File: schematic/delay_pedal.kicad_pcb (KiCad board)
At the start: 4 copper layers, 110 x 50 mm, 149 parts, among them J1 IN Gain, J10 VFLASH, J12 LP, J13 Mix, J14 OUT Gain, J3 SPI FLASH, J4 Audio In, J5 FDBK, J6 +9V, J8 Time, J9 Audio Out, SW1 RESET, SW2 SW_SPST, U1 ICE40LP1K-QN84, U10 TPL810ADJ-5TR, U11 TPL810F50-89TR, U12 ADS8339IDGSR, U13 TLV76033DBZR, U14 OPA1678, U15 DAC8551IADGKR, U16 REF5045AD, U17 OPA1678, U2 APS1604M-3SQR, U3 OPA1678, U4 NXB0104, U5 OPA1678, U6 W25X20CLSN, U8 OPA1678, U9 OPA1678, X1 KXO-V96T

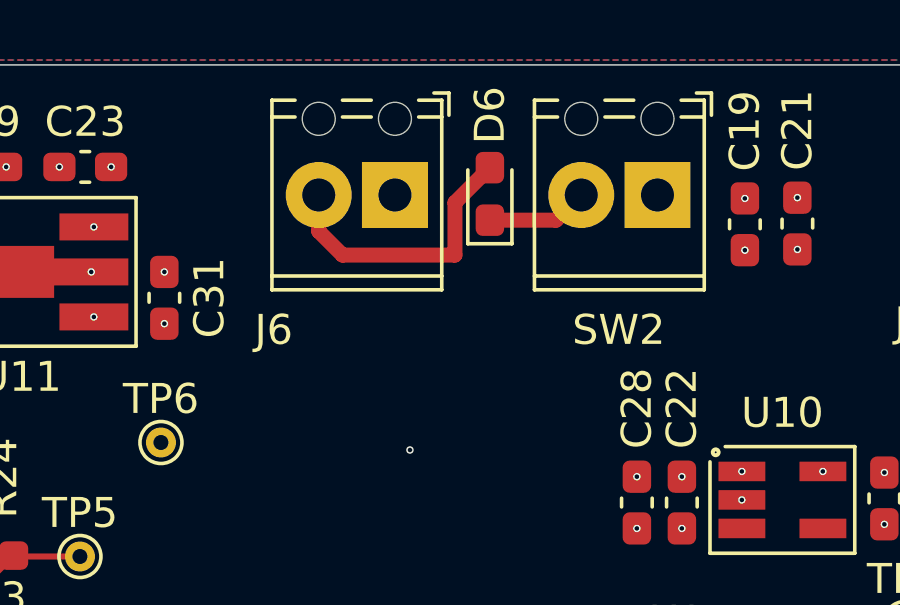
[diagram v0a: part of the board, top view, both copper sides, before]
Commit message: Updated Schottky diode footprint
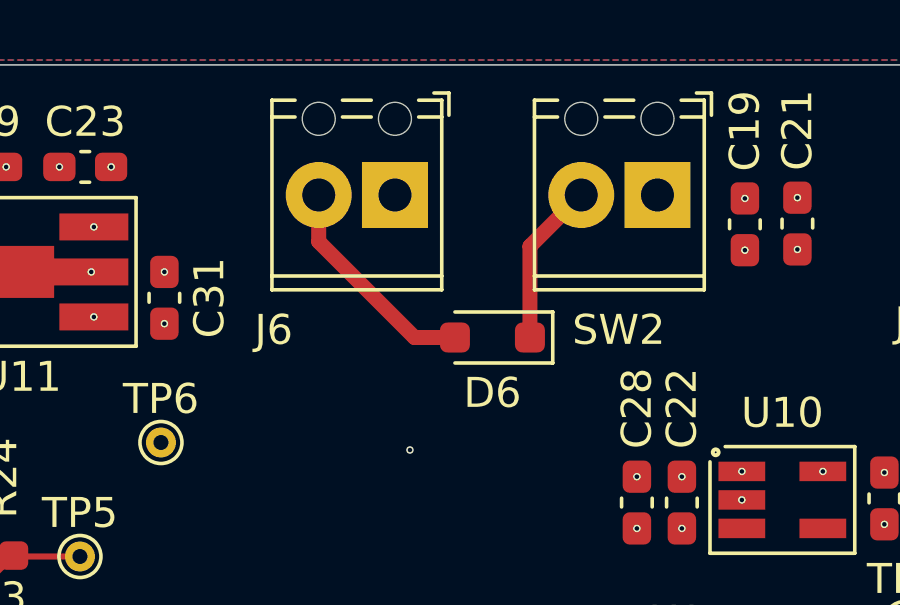
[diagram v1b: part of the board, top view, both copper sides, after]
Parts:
- D6: footprint Diode_SMD:D_0603_1608Metric_Pad1.05x0.95mm_HandSolder -> Diode_SMD:D_SOD-323_HandSoldering
- moved D6 4.79 mm to (166.2, 84.0), turned to 180 degrees
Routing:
- net Net-(D6-K): track 3.31 -> 5.49 mm
- net /+9V: track 10.1 -> 8.09 mm
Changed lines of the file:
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@@
 		)
 	)
-	(footprint "Diode_SMD:D_0603_1608Metric_Pad1.05x0.95mm_HandSolder"
+	(footprint "Diode_SMD:D_SOD-323_HandSoldering"
 		(layer "F.Cu")
-		(at 166.164214 79.214214 90)
-		(descr "Diode SMD 0603 (1608 Metric), square (rectangular) end terminal, IPC_7351 nominal, (Body size source: http://www.tortai-tech.com/upload/download/2011102023233369053.pdf), generated with kicad-footprint-generator")
-		(tags "diode handsolder")
+		(at 166.25 84 180)
+		(descr "SOD-323")
+		(tags "SOD-323")
 		(property "Reference" "D6"
-			(at 2.625 0 90)
+			(at 0 -1.85 360)
 			(layer "F.SilkS")
 			(effects
@@
 		)
 		(property "Value" "Schottky"
-			(at 0 1.43 90)
+			(at 0.1 1.9 360)
 			(layer "F.Fab")
 			(hide yes)
@@
 			)
 		)
-		(property "Footprint" "Diode_SMD:D_0603_1608Metric_Pad1.05x0.95mm_HandSolder"
-			(at 0 0 90)
+		(property "Footprint" "Diode_SMD:D_SOD-323_HandSoldering"
+			(at 0 0 180)
 			(unlocked yes)
 			(layer "F.Fab")
@@
 		)
 		(property "Datasheet" ""
-			(at 0 0 90)
+			(at 0 0 180)
 			(unlocked yes)
 			(layer "F.Fab")
@@
 		)
 		(property "Description" "Schottky diode, Generic Symbol, Alternate KiCAD Library"
-			(at 0 0 90)
+			(at 0 0 180)
 			(unlocked yes)
 			(layer "F.Fab")
@@
 		(attr smd)
 		(fp_line
-			(start 0.8 -0.735)
-			(end -1.66 -0.735)
+			(start -2.01 0.85)
+			(end 1.25 0.85)
 			(stroke
 				(width 0.12)
@@
 		)
 		(fp_line
-			(start -1.66 -0.735)
-			(end -1.66 0.735)
+			(start -2.01 -0.85)
+			(end 1.25 -0.85)
 			(stroke
 				(width 0.12)
@@
 		)
 		(fp_line
-			(start -1.66 0.735)
-			(end 0.8 0.735)
+			(start -2.01 -0.85)
+			(end -2.01 0.85)
 			(stroke
 				(width 0.12)
@@
 		)
 		(fp_line
-			(start 1.65 -0.73)
-			(end 1.65 0.73)
+			(start 2 -0.95)
+			(end 2 0.95)
 			(stroke
 				(width 0.05)
@@
 		)
 		(fp_line
-			(start -1.65 -0.73)
-			(end 1.65 -0.73)
+			(start -2 0.95)
+			(end 2 0.95)
 			(stroke
 				(width 0.05)
@@
 		)
 		(fp_line
-			(start 1.65 0.73)
-			(end -1.65 0.73)
+			(start -2 -0.95)
+			(end 2 -0.95)
 			(stroke
 				(width 0.05)
@@
 		)
 		(fp_line
-			(start -1.65 0.73)
-			(end -1.65 -0.73)
+			(start -2 -0.95)
+			(end -2 0.95)
 			(stroke
 				(width 0.05)
@@
 		)
 		(fp_line
-			(start 0.8 -0.4)
-			(end -0.5 -0.4)
+			(start 0.9 0.7)
+			(end -0.9 0.7)
 			(stroke
 				(width 0.1)
@@
 		)
 		(fp_line
-			(start -0.5 -0.4)
-			(end -0.8 -0.1)
+			(start 0.9 -0.7)
+			(end 0.9 0.7)
 			(stroke
 				(width 0.1)
@@
 		)
 		(fp_line
-			(start -0.8 -0.1)
-			(end -0.8 0.4)
+			(start 0.2 0.35)
+			(end -0.3 0)
 			(stroke
 				(width 0.1)
@@
 		)
 		(fp_line
-			(start 0.8 0.4)
-			(end 0.8 -0.4)
+			(start 0.2 0)
+			(end 0.45 0)
 			(stroke
 				(width 0.1)
@@
 		)
 		(fp_line
-			(start -0.8 0.4)
-			(end 0.8 0.4)
+			(start 0.2 -0.35)
+			(end 0.2 0.35)
+			(stroke
+				(width 0.1)
+				(type solid)
+			)
+			(layer "F.Fab")
+		)
+		(fp_line
+			(start -0.3 0)
+			(end 0.2 -0.35)
+			(stroke
+				(width 0.1)
+				(type solid)
+			)
+			(layer "F.Fab")
+		)
+		(fp_line
+			(start -0.3 0)
+			(end -0.5 0)
+			(stroke
+				(width 0.1)
+				(type solid)
+			)
+			(layer "F.Fab")
+		)
+		(fp_line
+			(start -0.3 -0.35)
+			(end -0.3 0.35)
+			(stroke
+				(width 0.1)
+				(type solid)
+			)
+			(layer "F.Fab")
+		)
+		(fp_line
+			(start -0.9 0.7)
+			(end -0.9 -0.7)
+			(stroke
+				(width 0.1)
+				(type solid)
+			)
+			(layer "F.Fab")
+		)
+		(fp_line
+			(start -0.9 -0.7)
+			(end 0.9 -0.7)
 			(stroke
 				(width 0.1)
@@
 		)
 		(fp_text user "${REFERENCE}"
-			(at 0 0 90)
+			(at 0 -1.85 360)
 			(layer "F.Fab")
 			(effects
 				(font
-					(size 0.4 0.4)
-					(thickness 0.06)
+					(size 1 1)
+					(thickness 0.15)
 				)
 			)
 		)
 		(pad "1" smd roundrect
-			(at -0.875 0 90)
-			(size 1.05 0.95)
+			(at -1.25 0 180)
+			(size 1 1)
 			(layers "F.Cu" "F.Paste" "F.Mask")
 			(roundrect_rratio 0.25)
@@
 		)
 		(pad "2" smd roundrect
-			(at 0.875 0 90)
-			(size 1.05 0.95)
+			(at 1.25 0 180)
+			(size 1 1)
 			(layers "F.Cu" "F.Paste" "F.Mask")
 			(roundrect_rratio 0.25)
@@
 			(pintype "passive")
 		)
-		(model "${KICAD8_3DMODEL_DIR}/Diode_SMD.3dshapes/D_0603_1608Metric.wrl"
+		(model "${KICAD8_3DMODEL_DIR}/Diode_SMD.3dshapes/D_SOD-323.wrl"
 			(offset
 				(xyz 0 0 0)
@@
 	)
 	(segment
-		(start 165 79.503428)
-		(end 165 81.2525)
-		(width 0.5)
-		(layer "F.Cu")
-		(net 32)
-	)
-	(segment
-		(start 160.46 80.46)
-		(end 160.46 79.25)
+		(start 163.654366 84)
+		(end 165 84)
 		(width 0.5)
 		(layer "F.Cu")
@@
 	)
 	(segment
-		(start 165 81.2525)
-		(end 161.2525 81.2525)
-		(width 0.5)
-		(layer "F.Cu")
-		(net 32)
-	)
-	(segment
-		(start 161.2525 81.2525)
-		(end 160.46 80.46)
+		(start 160.624214 79.299214)
+		(end 160.624214 78.625786)
 		(width 0.5)
 		(layer "F.Cu")
@@
 	)
 	(segment
-		(start 160.624214 79.299214)
-		(end 160.624214 78.625786)
+		(start 160.46 79.25)
+		(end 160.46 80.805634)
 		(width 0.5)
 		(layer "F.Cu")
@@
 	)
 	(segment
-		(start 166.164214 78.339214)
-		(end 165 79.503428)
+		(start 160.46 80.805634)
+		(end 163.654366 84)
 		(width 0.5)
 		(layer "F.Cu")
@@
 	)
 	(segment
-		(start 168.370786 80.089214)
-		(end 169.124214 79.335786)
+		(start 167.5 80.96)
+		(end 169.21 79.25)
 		(width 0.5)
 		(layer "F.Cu")
@@
 	)
 	(segment
-		(start 166.164214 80.089214)
-		(end 168.370786 80.089214)
+		(start 167.5 84)
+		(end 167.5 80.96)
 		(width 0.5)
 		(layer "F.Cu")

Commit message: Generated fabrication files
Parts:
- C19: footprint Capacitor_SMD:C_0603_1608Metric_Pad1.08x0.95mm_HandSolder -> Capacitor_THT:CP_Radial_D6.3mm_P2.50mm
- C40, C5, C60: footprint Capacitor_SMD:C_0603_1608Metric_Pad1.08x0.95mm_HandSolder -> Capacitor_SMD:C_1206_3216Metric_Pad1.33x1.80mm_HandSolder
- J1, J12, J14, J4, J5, J6, J9, SW2: footprint TerminalBlock_Phoenix:TerminalBlock_Phoenix_MPT-0,5-2-2.54_1x02_P2.54mm_Horizontal -> Connector_PinHeader_2.54mm:PinHeader_1x02_P2.54mm_Vertical
- J13: footprint TerminalBlock_Phoenix:TerminalBlock_Phoenix_MPT-0,5-3-2.54_1x03_P2.54mm_Horizontal -> Connector_PinHeader_2.54mm:PinHeader_1x03_P2.54mm_Vertical
- J8: footprint TerminalBlock_Phoenix:TerminalBlock_Phoenix_MPT-0,5-5-2.54_1x05_P2.54mm_Horizontal -> Connector_PinHeader_2.54mm:PinHeader_1x05_P2.54mm_Vertical
- U14, U17, U3, U5, U8, U9: value OPA1678 -> RC4580
- moved TP1 5.48 mm to (102.5, 112.7)
- moved C21 4.18 mm to (172.6, 82.0), turned to 0 degrees
- moved C19 3.40 mm to (178.0, 79.6), turned to -90 degrees
- moved J8 2.75 mm to (194.5, 79.2), turned to -90 degrees
- moved C60 1.78 mm to (151.9, 103.2), turned to 90 degrees
- moved C40 0.95 mm to (114.6, 90.2)
- moved C5 0.90 mm to (107.1, 109.8)
- turned J1 to 90 degrees
- turned J12 to 90 degrees
- turned J13 to 0 degrees
- turned J14 to -90 degrees
- turned J4 to 0 degrees
- turned J5 to 90 degrees
- turned J6 to -90 degrees
- turned J9 to 0 degrees
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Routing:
- net Net-(J12-Pin_1): track 27.5 -> 24.8 mm
- net Net-(J5-Pin_2): track 7.38 -> 5.90 mm
- net Net-(J14-Pin_2): track 13.3 -> 14.8 mm
- net Aref: track 22.2 -> 20.7 mm
- net /IN: track 13.8 -> 12.5 mm
- net /FLASH.SCK: track 22.8 -> 21.7 mm
- net /FLASH.SDI: track 22.0 -> 21.1 mm
- net Net-(U3A-+): track 5.63 -> 6.41 mm
- net /FLASH.SDO: track 24.1 -> 24.8 mm
- net /OUT: track 22.7 -> 22.2 mm
- net Vs: vias 26 -> 25

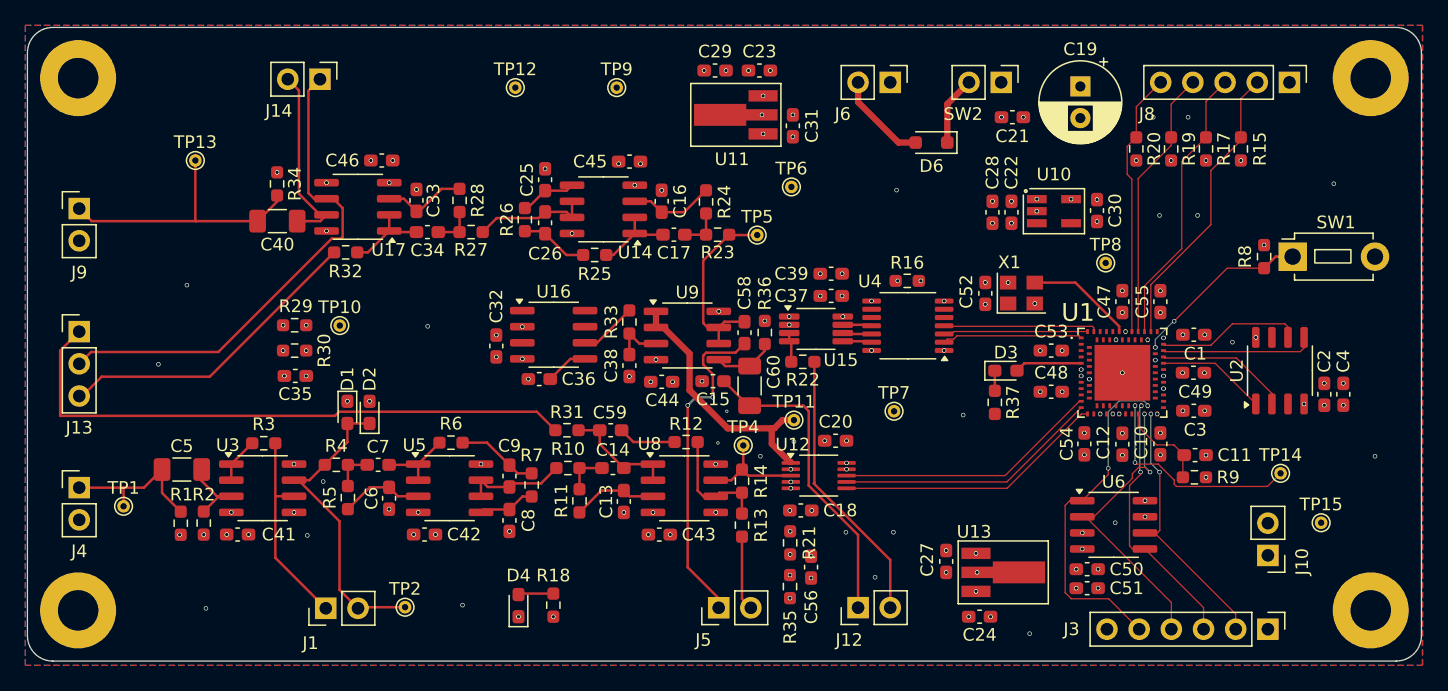
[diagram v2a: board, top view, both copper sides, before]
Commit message: Fixed footprint assignments
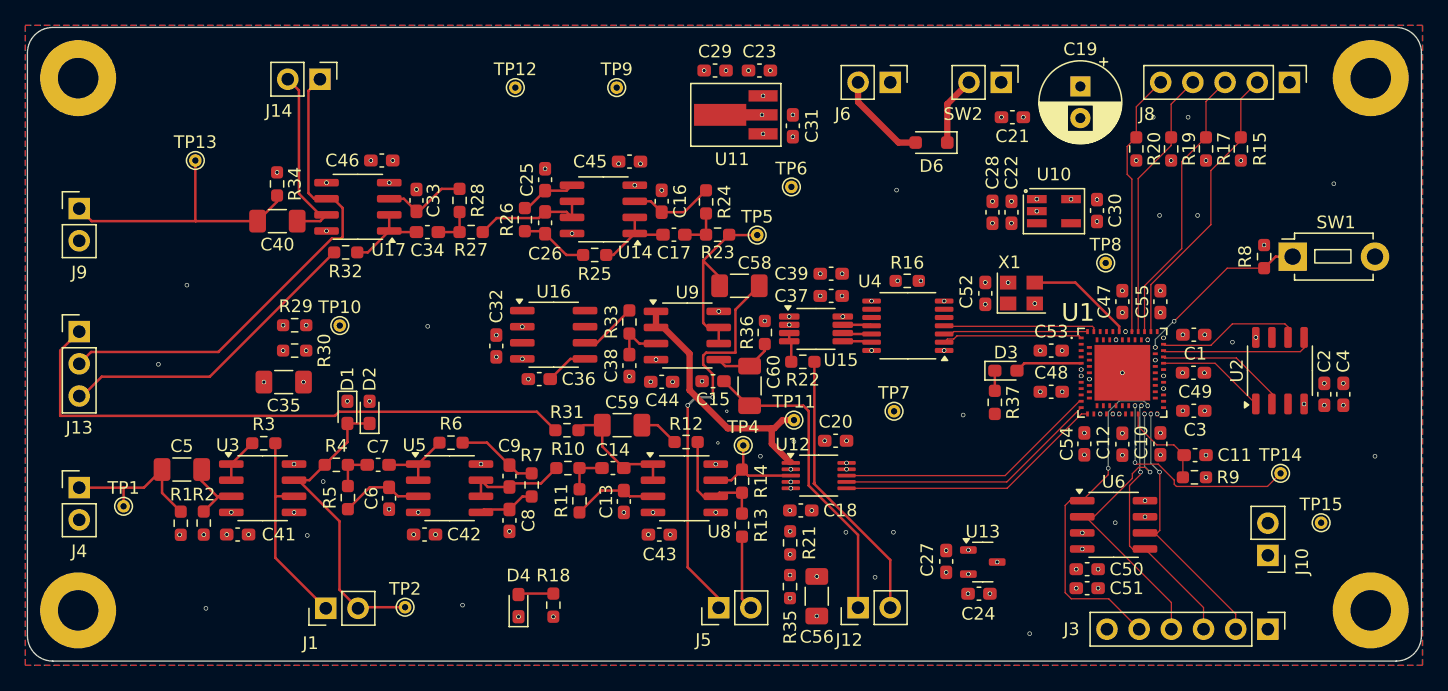
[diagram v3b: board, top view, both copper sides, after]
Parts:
- C35, C56, C58, C59: footprint Capacitor_SMD:C_0603_1608Metric_Pad1.08x0.95mm_HandSolder -> Capacitor_SMD:C_1206_3216Metric_Pad1.33x1.80mm_HandSolder
- U13: footprint PCM_Package_TO_SOT_SMD_AKL:SOT-89-3_Handsoldering -> Package_TO_SOT_SMD:SOT-23-3
- moved C58 3.72 mm to (151.1, 95.3), turned to 180 degrees
- moved C56 2.34 mm to (157.2, 119.8)
- moved C24 1.81 mm to (170.0, 119.6), turned to 0 degrees
- moved U13 1.81 mm to (170.3, 117.1)
- moved C35 1.04 mm to (115.1, 102.9)
- moved C59 0.98 mm to (141.8, 106.3)
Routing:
- net Net-(J5-Pin_1): track 26.5 -> 31.5 mm
- net Net-(C59-Pad1): track 4.61 -> 3.17 mm
- net Net-(U8A--): track 9.15 -> 9.93 mm

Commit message: Moved power supply LED close to power supply input
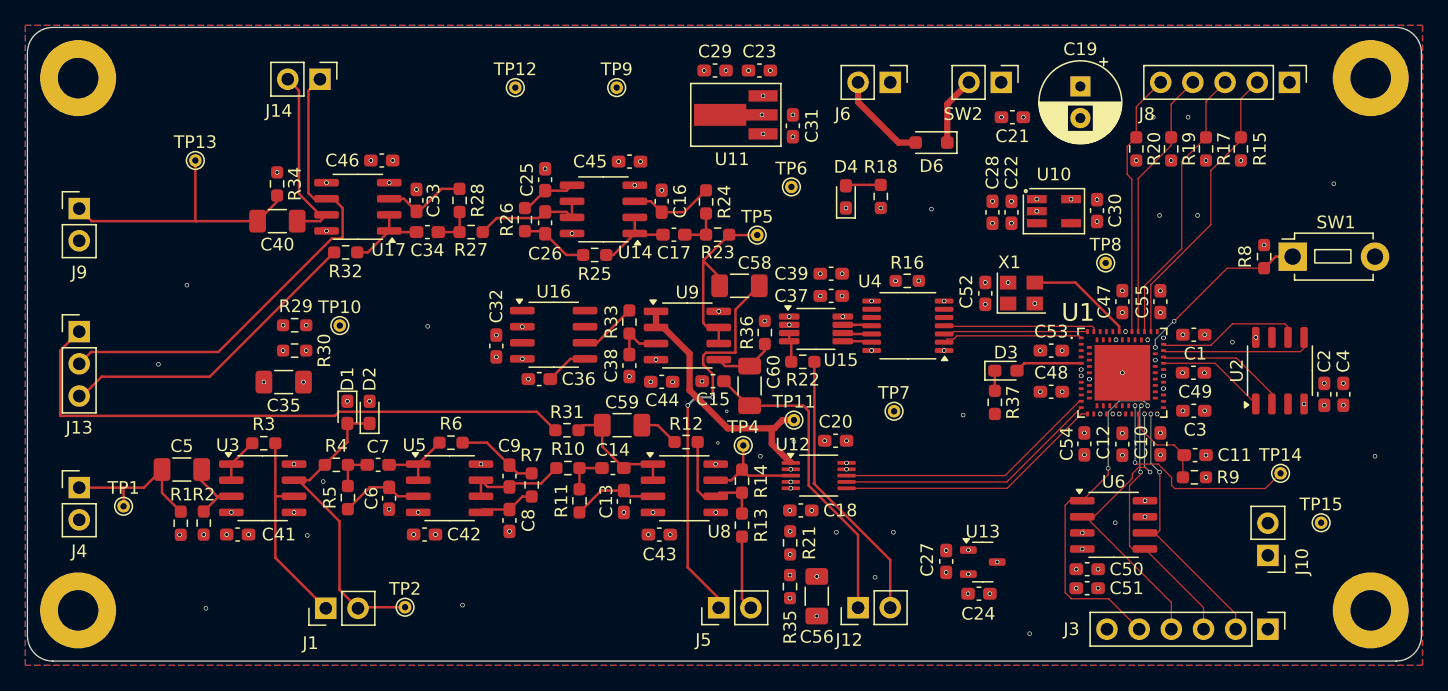
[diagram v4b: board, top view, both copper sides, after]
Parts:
- moved D4 41.3 mm to (159.5, 88.3)
- moved R18 41.3 mm to (162.2, 88.2)
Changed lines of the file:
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@@
 	(footprint "LED_SMD:LED_0603_1608Metric_Pad1.05x0.95mm_HandSolder"
 		(layer "F.Cu")
-		(at 133.664214 120.539214 90)
+		(at 159.5 88.2875 90)
 		(descr "LED SMD 0603 (1608 Metric), square (rectangular) end terminal, IPC_7351 nominal, (Body size source: http://www.tortai-tech.com/upload/download/2011102023233369053.pdf), generated with kicad-footprint-generator")
 		(tags "LED handsolder")
@@
 		(tags "capacitor handsolder")
 		(property "Reference" "C24"
-			(at -0.051714 1.585786 360)
+			(at -0.051714 1.585786 0)
 			(layer "F.SilkS")
 			(effects
@@
 		)
 		(property "Value" "1u"
-			(at 0 1.43 360)
+			(at 0 1.43 0)
 			(layer "F.Fab")
 			(hide yes)
@@
 		)
 		(fp_text user "${REFERENCE}"
-			(at 0 0 360)
+			(at 0 0 0)
 			(layer "F.Fab")
 			(effects
@@
 	(footprint "Resistor_SMD:R_0603_1608Metric_Pad0.98x0.95mm_HandSolder"
 		(layer "F.Cu")
-		(at 136.414214 120.501714 90)
+		(at 162.25 88.25 90)
 		(descr "Resistor SMD 0603 (1608 Metric), square (rectangular) end terminal, IPC_7351 nominal with elongated pad for handsoldering. (Body size source: IPC-SM-782 page 72, https://www.pcb-3d.com/wordpress/wp-content/uploads/ipc-sm-782a_amendment_1_and_2.pdf), generated with kicad-footprint-generator")
 		(tags "resistor handsolder")
@@
 	)
 	(via
-		(at 143.289214 85.669214)
+		(at 143.289214 85.5)
 		(size 0.35)
 		(drill 0.25)
@@
 	)
 	(via
-		(at 165.414214 94.914214)
+		(at 165.25 94.914214)
 		(size 0.35)
 		(drill 0.25)
@@
 	)
 	(via
-		(at 159.5 114.75)
+		(at 158.75 114.75)
 		(size 0.35)
 		(drill 0.25)
@@
 	)
 	(via
-		(at 163.5 87.75)
+		(at 166.25 89.25)
 		(size 0.35)
 		(drill 0.25)
@@
 	)
 	(via
-		(at 133.664214 121.414214)
+		(at 159.5 89.1625)
 		(size 0.35)
 		(drill 0.25)
@@
 	)
 	(via
-		(at 163.589214 94.914214)
+		(at 163.425 94.914214)
 		(size 0.35)
 		(drill 0.25)
@@
 	)
 	(via
-		(at 141.564214 85.669214)
+		(at 141.564214 85.5)
 		(size 0.35)
 		(drill 0.25)
@@
 	)
 	(via
-		(at 136.414214 121.414214)
+		(at 162.25 89.1625)
 		(size 0.35)
 		(drill 0.25)
@@
 	)
 	(segment
-		(start 136.414214 119.589214)
-		(end 133.739214 119.589214)
+		(start 162.25 87.3375)
+		(end 159.575 87.3375)
 		(width 0.2)
 		(layer "F.Cu")
@@
 	)
 	(segment
-		(start 133.739214 119.589214)
-		(end 133.664214 119.664214)
+		(start 159.575 87.3375)
+		(end 159.5 87.4125)
 		(width 0.2)
 		(layer "F.Cu")
@@
 	)
 	(segment
-		(start 184.144974 109.371714)
-		(end 182.435928 109.371714)
+		(start 185.45 111.3)
+		(end 185.2 111.05)
 		(width 0.09)
 		(layer "F.Cu")
@@
 	)
 	(segment
-		(start 185.406714 110.958152)
-		(end 185.582776 111.134214)
+		(start 192.6 111.3)
+		(end 185.45 111.3)
 		(width 0.09)
 		(layer "F.Cu")
@@
 	)
 	(segment
-		(start 185.406714 110.633454)
+		(start 185.2 110.42674)
 		(end 184.144974 109.371714)
 		(width 0.09)
@@
 	)
 	(segment
-		(start 185.406714 110.633454)
-		(end 185.406714 110.958152)
+		(start 184.144974 109.371714)
+		(end 182.435928 109.371714)
 		(width 0.09)
 		(layer "F.Cu")
@@
 	)
 	(segment
-		(start 192.765786 111.134214)
-		(end 193.8 110.1)
+		(start 182.435928 109.371714)
+		(end 182.314214 109.25)
 		(width 0.09)
 		(layer "F.Cu")
@@
 	)
 	(segment
-		(start 182.435928 109.371714)
-		(end 182.314214 109.25)
+		(start 185.2 111.05)
+		(end 185.2 110.42674)
 		(width 0.09)
 		(layer "F.Cu")
@@
 	)
 	(segment
-		(start 185.582776 111.134214)
-		(end 192.765786 111.134214)
+		(start 193.8 110.1)
+		(end 192.6 111.3)
 		(width 0.09)
 		(layer "F.Cu")

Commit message: Added silkscreen art
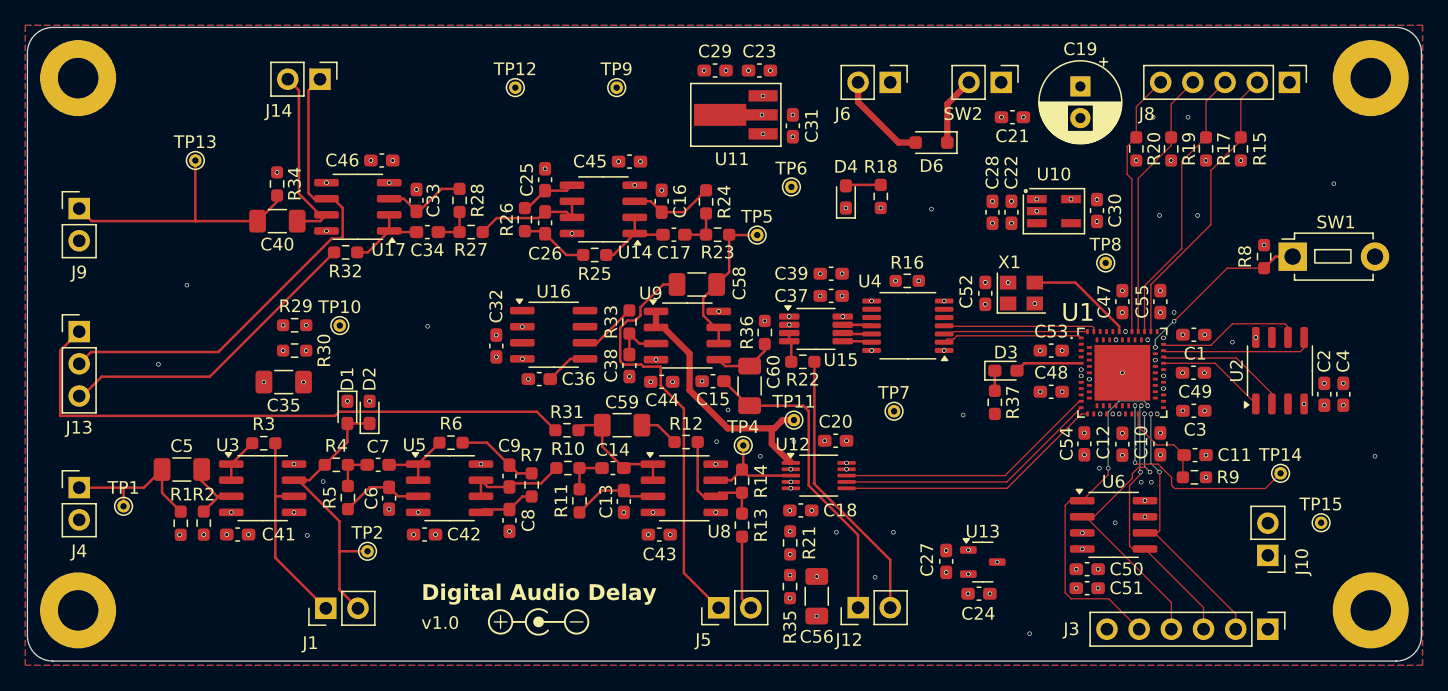
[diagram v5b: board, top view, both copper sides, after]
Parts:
- added REF**: Symbol_Barrel_Polarity, Symbol:Symbol_Barrel_Polarity, F.Cu at (135.2, 121.8)
- moved TP2 5.32 mm to (121.8, 116.2)
- moved C58 3.36 mm to (147.7, 95.2), turned to 0 degrees
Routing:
- net Net-(J5-Pin_1): track 31.5 -> 34.0 mm, vias 2 -> 0
- net Net-(D1-A): track 24.8 -> 23.4 mm
- net Net-(U9B--): track 15.7 -> 14.4 mm
- net GND: vias 100 -> 102
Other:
- board text added: "Digital Audio Delay"
- board text added: "v1.0"
